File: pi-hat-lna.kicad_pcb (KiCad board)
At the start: 4 copper layers, 65 x 56 mm, 109 parts, among them J1 USB_B_Mini, J3 DNF, J4 VAL**, J5 VAL**, J6 2x3 0.1" HEADER, J7 VAL**, J8 VAL**, J9 CONN_01X02, M1 2118706-2, M2 2118706-2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

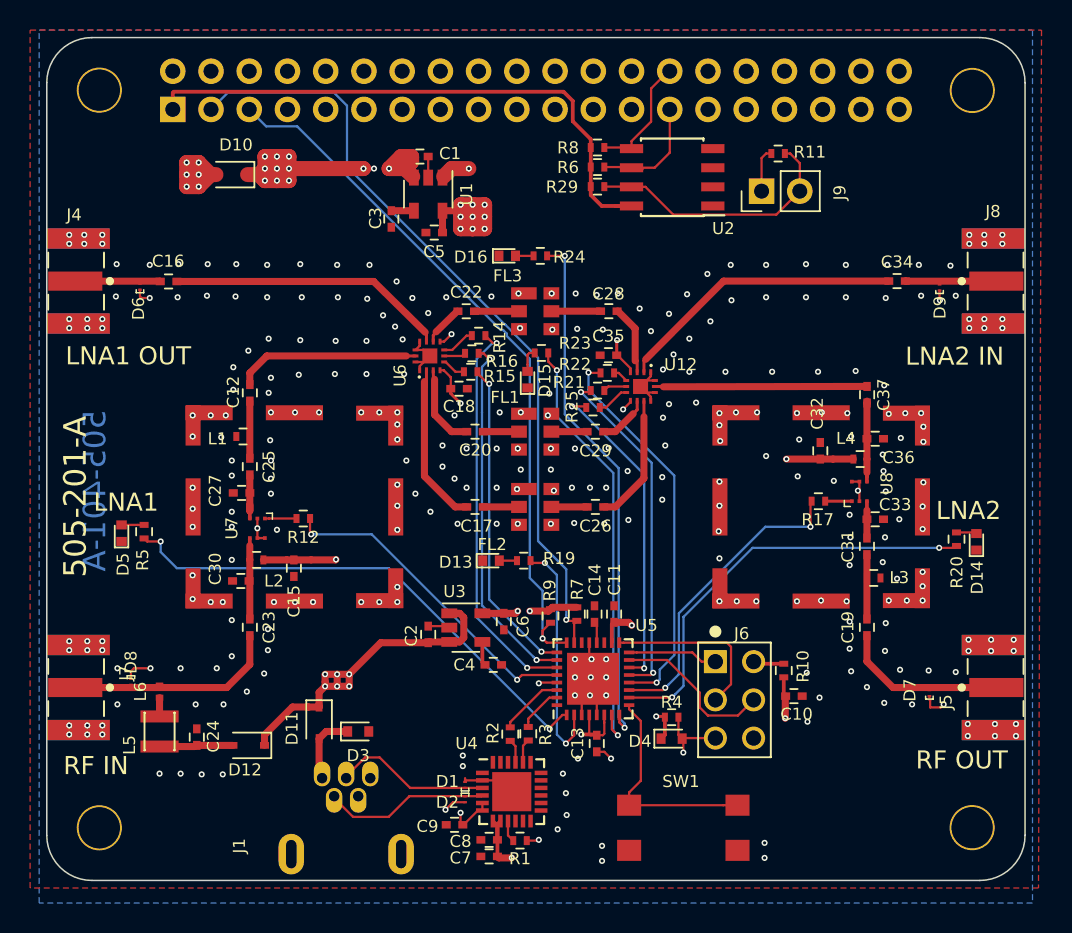
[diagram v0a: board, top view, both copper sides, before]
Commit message: Changed the 50 Ohm traces from 18.5 mils to 16 mils in order to accomodate one of the standard 4 layer stackups available from PCBWay.
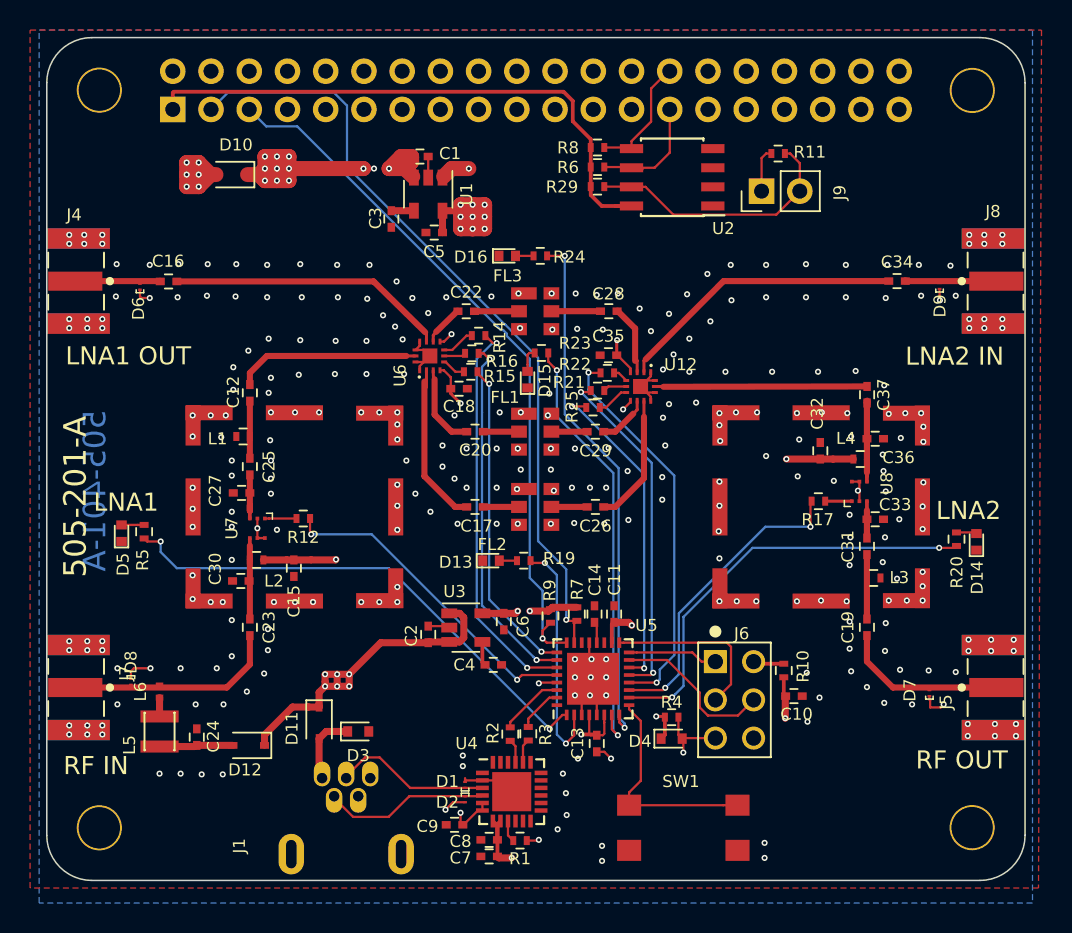
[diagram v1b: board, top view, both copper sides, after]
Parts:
- moved D9 0.10 mm to (137.9, 77.3)
